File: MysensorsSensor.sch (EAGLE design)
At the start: 41 parts, among them IC1 TS5205, IC2 AT25DF512C-SSHN-B, IC3 ATSHA204A, Q1 FC-12M, U1 ATMEGA328P-AU

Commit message: 1. fix wrong boost converter footprint 2. connect led to A1 pin instead of A2 (which was used by the boost converter enable 3. change crystal footrint but not change the pcb
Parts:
- removed C11: 10u, rcl:C-EUC0603K
- removed Q1: FC-12M, crystal:FC-12M
- removed U$1: MCP1640, pulseoxparts:MCP1640
- added IC4: MCP1640CT-I/CHY, Microchip_By_element14_Batch_1:MCP1640CT-I/CHY
- added Q2: (no value), crystal:CRYSTALCTS406
- added R11: 1M, resistor:R-US_R0603
- C10, C4, C5, C6, C7: value (none) -> 100n
- C12: value (none) -> 10n
- C8, C9: value 10u -> 22p
- CR123A: value (none) -> BAT_PACKCR123A; device Battery:TAKACHI_BATT-CR123A -> batteries:BAT_PACKCR123A
- CR2032: value (none) -> 3V
- L1: value (none) -> 4.7u
- R1, R2, R3, R5, R7: value 100k -> 1M
- R10, R9: value 100k -> 10k
- R4: value 100k -> 620k
- R8: value 100k -> 1k
- renumbered LED1 to D1, P1 to X1, S1 to RST, S2 to BTN, SJ1 to J1, SJ2 to J2, SV4 to X2, U1 to IC5
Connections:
- net A1: now also R8.2
- net A2: now also IC4.EN, R11.1; no longer R8.2, U$1.EN
- net GND: now also IC4.GND, R11.2; no longer C11.2, U$1.GND
- net N$1: now also IC4.VFB; no longer U$1.VFB
- net N$2: now also Q2.1; no longer Q1.1
- net N$4: now also IC4.SW; no longer U$1.SW
- net N$6: now also Q2.2; no longer Q1.2
- net VBAT: now also IC4.VIN; no longer C11.1, U$1.VIN
- net VBOOST: now also IC4.VOUT; no longer U$1.VOUT
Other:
- moved on the sheet: C2, C3, CR123A, L1, R3, R4

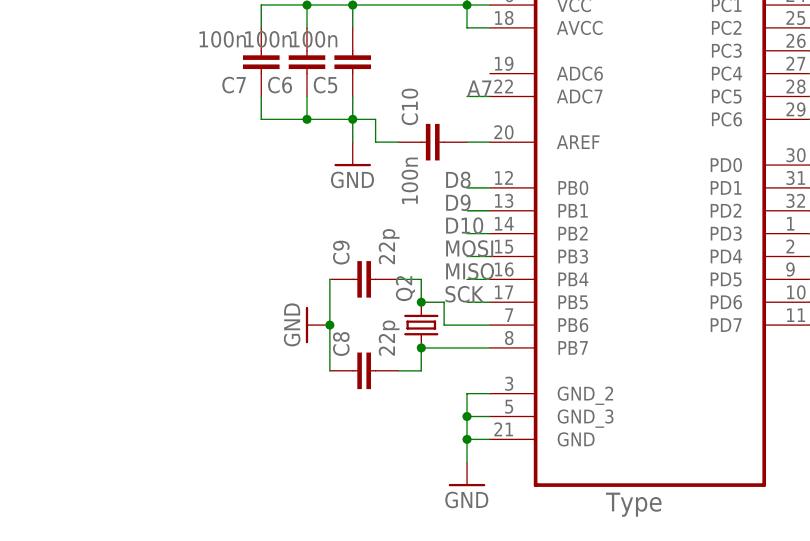
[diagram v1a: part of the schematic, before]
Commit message: 1. rearrange nfr24l01 connector and atmega328p chip
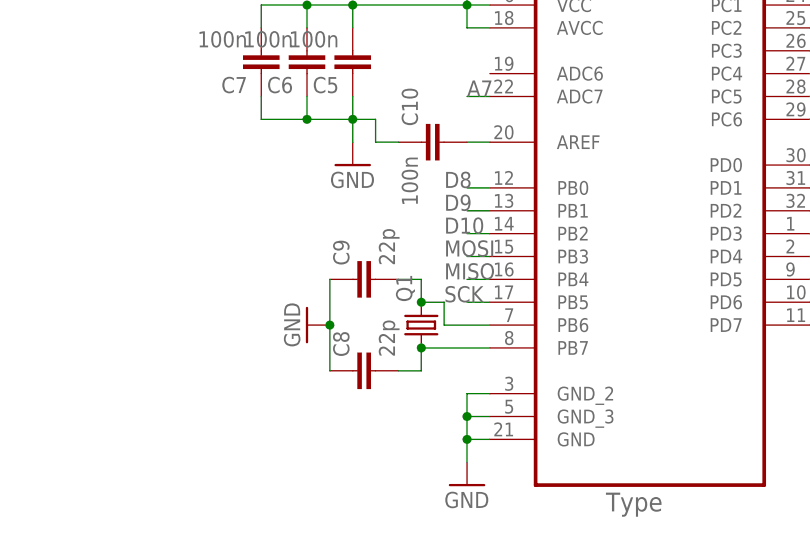
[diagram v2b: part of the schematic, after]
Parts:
- renumbered Q2 to Q1
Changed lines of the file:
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@@
 <part name="GND13" library="supply1" deviceset="GND" device=""/>
 <part name="IC4" library="Microchip_By_element14_Batch_1" deviceset="MCP1640CT-I/CHY" device=""/>
-<part name="Q2" library="crystal" deviceset="CRYSTAL" device="CTS406"/>
+<part name="Q1" library="crystal" deviceset="CRYSTAL" device="CTS406"/>
 </parts>
 <sheets>
@@
 <instance part="GND13" gate="1" x="-25.4" y="78.74"/>
 <instance part="IC4" gate="A" x="0" y="99.06"/>
-<instance part="Q2" gate="G$1" x="40.64" y="30.48" rot="R90"/>
+<instance part="Q1" gate="G$1" x="40.64" y="30.48" rot="R90"/>
 </instances>
 <busses>
@@
 <pinref part="C8" gate="G$1" pin="2"/>
 <wire x1="40.64" y1="25.4" x2="38.1" y2="25.4" width="0.1524" layer="91"/>
-<pinref part="Q2" gate="G$1" pin="1"/>
+<pinref part="Q1" gate="G$1" pin="1"/>
 <junction x="40.64" y="27.94"/>
 </segment>
@@
 <pinref part="C9" gate="G$1" pin="2"/>
 <wire x1="40.64" y1="35.56" x2="38.1" y2="35.56" width="0.1524" layer="91"/>
-<pinref part="Q2" gate="G$1" pin="2"/>
+<pinref part="Q1" gate="G$1" pin="2"/>
 <junction x="40.64" y="33.02"/>
 </segment>

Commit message: connect radio module irq with d2
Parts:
- IC1: value TS5205 -> APE8865Y5-30-HF-3
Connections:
- net D2: now also NRF24L01.IRQ
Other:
- moved on the sheet: C12, C13
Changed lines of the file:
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@@
 <part name="P+9" library="supply1" deviceset="VCC" device=""/>
 <part name="GND9" library="supply1" deviceset="GND" device=""/>
-<part name="IC1" library="v-reg" deviceset="TS5205" device=""/>
+<part name="IC1" library="v-reg" deviceset="TS5205" device="" value="APE8865Y5-30-HF-3"/>
 <part name="GND10" library="supply1" deviceset="GND" device=""/>
 <part name="C12" library="rcl" deviceset="C-EU" device="C0402" value="10n"/>
@@
 <instance part="IC1" gate="G$1" x="30.48" y="149.86"/>
 <instance part="GND10" gate="1" x="12.7" y="142.24"/>
-<instance part="C12" gate="G$1" x="43.18" y="142.24" rot="R180"/>
-<instance part="GND11" gate="1" x="43.18" y="137.16"/>
-<instance part="C13" gate="G$1" x="50.8" y="147.32"/>
+<instance part="C12" gate="G$1" x="53.34" y="142.24" rot="R180"/>
+<instance part="GND11" gate="1" x="53.34" y="137.16"/>
+<instance part="C13" gate="G$1" x="58.42" y="147.32"/>
 <instance part="P+2" gate="VCC" x="86.36" y="139.7"/>
 <instance part="C14" gate="G$1" x="12.7" y="152.4"/>
@@
 <pinref part="GND11" gate="1" pin="GND"/>
 <pinref part="C13" gate="G$1" pin="2"/>
-<wire x1="50.8" y1="142.24" x2="50.8" y2="139.7" width="0.1524" layer="91"/>
-<wire x1="50.8" y1="139.7" x2="43.18" y2="139.7" width="0.1524" layer="91"/>
-<junction x="43.18" y="139.7"/>
+<wire x1="58.42" y1="142.24" x2="58.42" y2="139.7" width="0.1524" layer="91"/>
+<wire x1="58.42" y1="139.7" x2="53.34" y2="139.7" width="0.1524" layer="91"/>
+<junction x="53.34" y="139.7"/>
 </segment>
 <segment>
@@
 <wire x1="129.54" y1="43.18" x2="129.54" y2="53.34" width="0.1524" layer="91"/>
 <label x="86.36" y="43.18" size="1.778" layer="95"/>
+<pinref part="NRF24L01" gate="G$1" pin="IRQ"/>
+<wire x1="165.1" y1="78.74" x2="139.7" y2="78.74" width="0.1524" layer="91"/>
+<wire x1="139.7" y1="78.74" x2="139.7" y2="43.18" width="0.1524" layer="91"/>
+<wire x1="139.7" y1="43.18" x2="129.54" y2="43.18" width="0.1524" layer="91"/>
+<junction x="129.54" y="43.18"/>
 </segment>
 </net>
@@
 <pinref part="IC1" gate="G$1" pin="CB"/>
 <pinref part="C12" gate="G$1" pin="2"/>
-<wire x1="40.64" y1="147.32" x2="43.18" y2="147.32" width="0.1524" layer="91"/>
+<wire x1="40.64" y1="147.32" x2="53.34" y2="147.32" width="0.1524" layer="91"/>
 </segment>
 </net>
@@
 <segment>
 <pinref part="IC1" gate="G$1" pin="VOUT"/>
-<label x="43.18" y="154.94" size="1.778" layer="95"/>
+<label x="58.42" y="154.94" size="1.778" layer="95"/>
 <pinref part="C13" gate="G$1" pin="1"/>
-<wire x1="40.64" y1="154.94" x2="50.8" y2="154.94" width="0.1524" layer="91"/>
-<wire x1="50.8" y1="154.94" x2="50.8" y2="149.86" width="0.1524" layer="91"/>
-</segment>
-<segment>
+<wire x1="40.64" y1="154.94" x2="58.42" y2="154.94" width="0.1524" layer="91"/>
+<wire x1="58.42" y1="154.94" x2="58.42" y2="149.86" width="0.1524" layer="91"/>
+</segment>
+<segment>

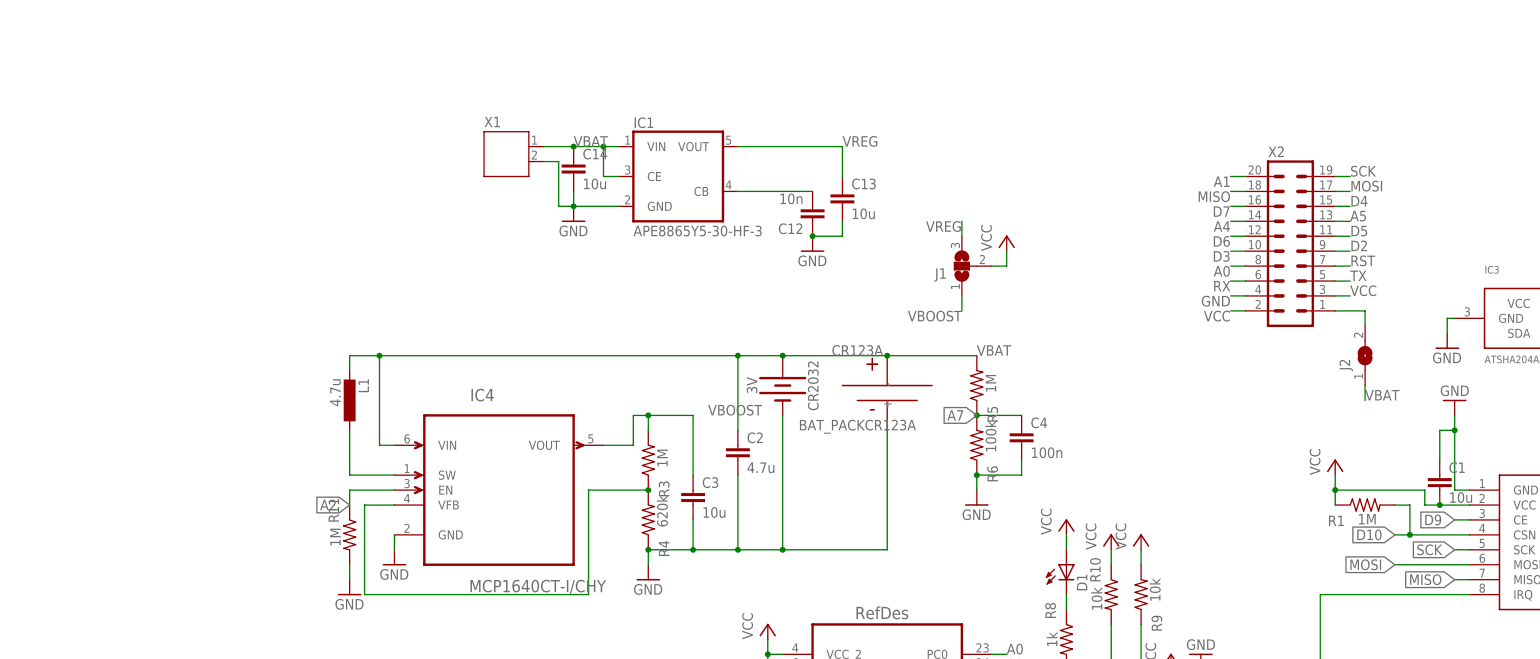
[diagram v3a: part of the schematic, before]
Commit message: use p-mosfet for reverse polarity
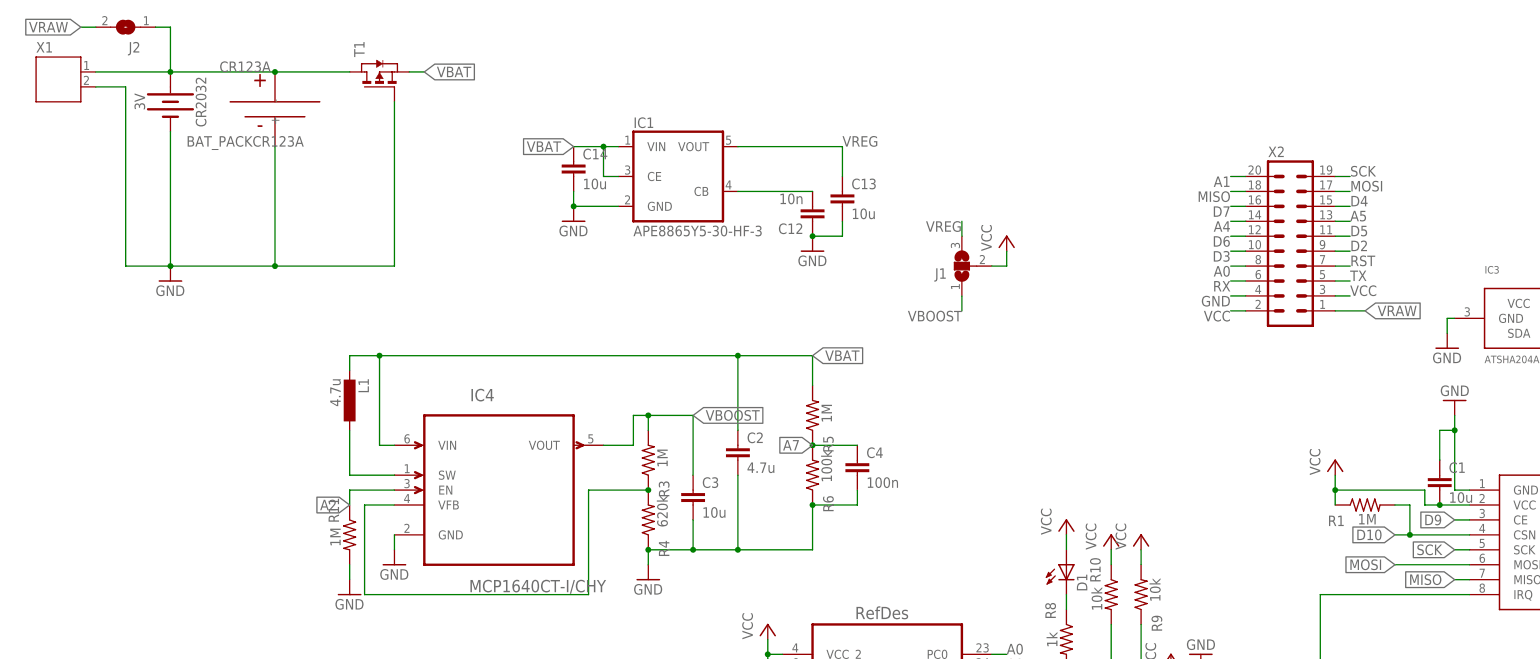
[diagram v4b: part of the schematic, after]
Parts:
- added T1: (no value), zetex:PMOSSOT23
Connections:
- net N$5 renamed VRAW
- new net N$7: CR123A.+, CR2032.+, J2.1, T1.D, X1.1
- net GND: now also T1.G
- net VBAT: now also T1.S; no longer CR123A.+, CR2032.+, J2.1, X1.1
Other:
- moved on the sheet: C4, CR123A, CR2032, J2, R5, R6, X1

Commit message: add RFM69
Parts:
- removed T1: (no value), zetex:PMOSSOT23
- added ANT: WIREPAD2,15/1,0, wirepad:WIREPAD2,15/1,0
- added Q2: FA-128, crystal:FA-128
- added RFM69W: RFM69HW, hoperf:RFM69HW
- C8, C9: device SparkFun-Passives:CAP0603-CAP -> SparkFun-Passives:CAP0402-CAP
- CR2032: value 3V -> (none); device SparkFun-Batteries:BATTERY-20MM_PTH -> Wurth_Elektronik_Electromechanic_Assembly_Spacer_rev15d:WA-BCPH_SMT_79527141
- Q1: device crystal:CRYSTALCTS406 -> zetex:PMOSSOT23
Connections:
- new net N$5: ANT.P, RFM69W.ANT
- net D10: now also RFM69W.NSS
- net D2: now also RFM69W.DIO0
- net GND: now also CR2032.NEG, Q1.G, Q2.2, Q2.4, RFM69W.GNDA, RFM69W.GNDB; no longer CR2032.-, T1.G
- net MISO: now also RFM69W.MISO
- net MOSI: now also RFM69W.MOSI
- net N$2: now also Q2.3; no longer Q1.1
- net N$6: now also Q2.1; no longer Q1.2
- net N$7: now also CR2032.POS, Q1.D; no longer CR2032.+, T1.D
- net SCK: now also RFM69W.SCK
- net VBAT: now also Q1.S; no longer T1.S
- net VCC: now also RFM69W.VCC
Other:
- moved on the sheet: C8, C9

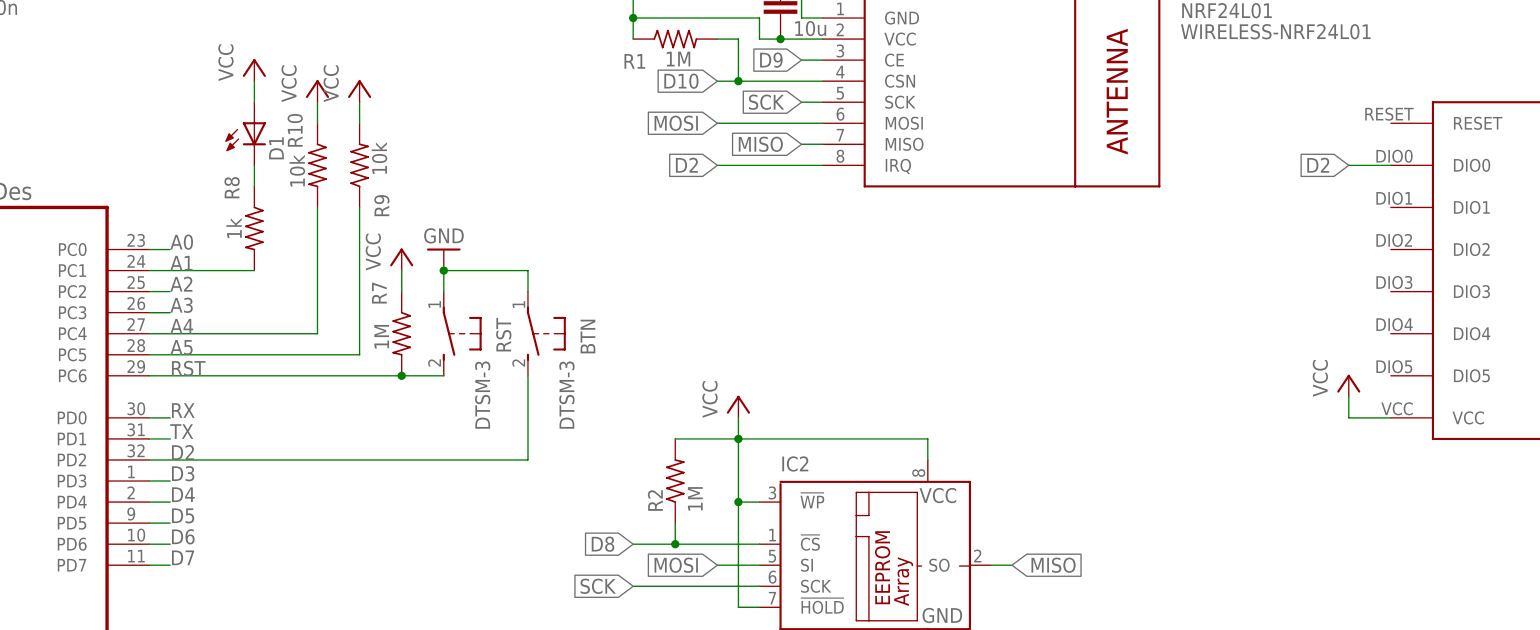
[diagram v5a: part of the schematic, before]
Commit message: add 0Ohm resistor for radio module interrupt + connect button to D3
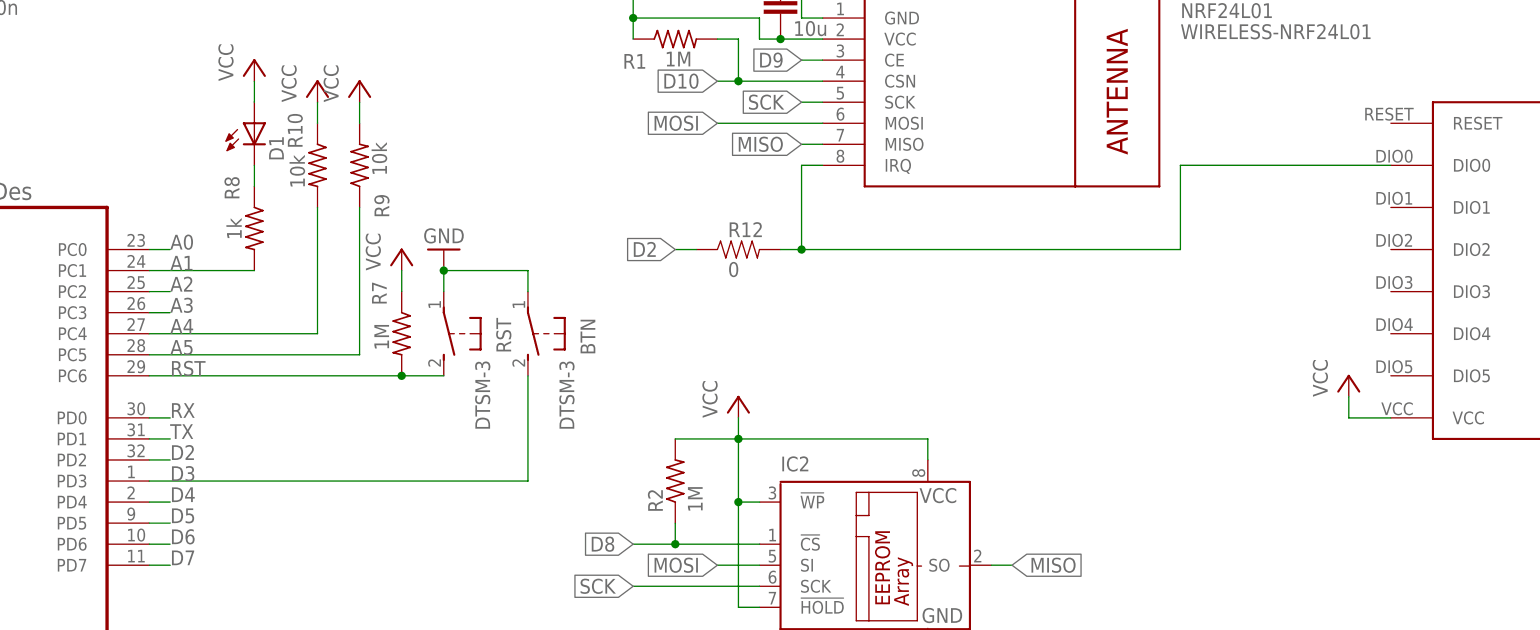
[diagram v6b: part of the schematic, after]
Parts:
- added R12: 0, SparkFun-Passives:RESISTOR0603-RES
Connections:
- new net N$9: NRF24L01.IRQ, R12.2, RFM69W.DIO0
- net D2: now also R12.1; no longer BTN.2, NRF24L01.IRQ, RFM69W.DIO0
- net D3: now also BTN.2
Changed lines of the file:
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@@
 <part name="CR2032" library="Wurth_Elektronik_Electromechanic_Assembly_Spacer_rev15d" deviceset="WA-BCPH" device="_SMT_79527141"/>
 <part name="Q2" library="crystal" deviceset="FA-" device="128"/>
+<part name="R12" library="SparkFun-Passives" deviceset="RESISTOR" device="0603-RES" value="0"/>
 </parts>
 <sheets>
@@
 <instance part="CR2032" gate="G$1" x="-55.88" y="152.4" rot="R270"/>
 <instance part="Q2" gate="G$1" x="38.1" y="30.48" rot="R270"/>
+<instance part="R12" gate="G$1" x="154.94" y="68.58" smashed="yes">
+<attribute name="NAME" x="153.67" y="70.0786" size="1.778" layer="95"/>
+<attribute name="VALUE" x="153.67" y="65.278" size="1.778" layer="96"/>
+</instance>
 </instances>
 <busses>
@@
 <segment>
 <pinref part="IC5" gate="A" pin="PD2"/>
-<pinref part="BTN" gate="G$1" pin="2"/>
-<wire x1="83.82" y1="43.18" x2="129.54" y2="43.18" width="0.1524" layer="91"/>
-<wire x1="129.54" y1="43.18" x2="129.54" y2="53.34" width="0.1524" layer="91"/>
+<wire x1="83.82" y1="43.18" x2="86.36" y2="43.18" width="0.1524" layer="91"/>
 <label x="86.36" y="43.18" size="1.778" layer="95"/>
 </segment>
 <segment>
-<pinref part="RFM69W" gate="A" pin="DIO0"/>
-<wire x1="233.68" y1="78.74" x2="228.6" y2="78.74" width="0.1524" layer="91"/>
-<label x="228.6" y="78.74" size="1.778" layer="95" rot="R180" xref="yes"/>
-</segment>
-<segment>
-<pinref part="NRF24L01" gate="G$1" pin="IRQ"/>
-<wire x1="165.1" y1="78.74" x2="152.4" y2="78.74" width="0.1524" layer="91"/>
-<label x="152.4" y="78.74" size="1.778" layer="95" rot="R180" xref="yes"/>
+<pinref part="R12" gate="G$1" pin="1"/>
+<wire x1="149.86" y1="68.58" x2="147.32" y2="68.58" width="0.1524" layer="91"/>
+<label x="147.32" y="68.58" size="1.778" layer="95" rot="R180" xref="yes"/>
 </segment>
 </net>
@@
 <segment>
 <pinref part="IC5" gate="A" pin="PD3"/>
-<wire x1="83.82" y1="40.64" x2="86.36" y2="40.64" width="0.1524" layer="91"/>
 <label x="86.36" y="40.64" size="1.778" layer="95"/>
+<pinref part="BTN" gate="G$1" pin="2"/>
+<wire x1="83.82" y1="40.64" x2="129.54" y2="40.64" width="0.1524" layer="91"/>
+<wire x1="129.54" y1="40.64" x2="129.54" y2="53.34" width="0.1524" layer="91"/>
 </segment>
 </net>
@@
 </segment>
 </net>
+<net name="N$9" class="0">
+<segment>
+<pinref part="RFM69W" gate="A" pin="DIO0"/>
+<wire x1="233.68" y1="78.74" x2="208.28" y2="78.74" width="0.1524" layer="91"/>
+<wire x1="208.28" y1="78.74" x2="208.28" y2="68.58" width="0.1524" layer="91"/>
+<pinref part="R12" gate="G$1" pin="2"/>
+<wire x1="208.28" y1="68.58" x2="162.56" y2="68.58" width="0.1524" layer="91"/>
+<pinref part="NRF24L01" gate="G$1" pin="IRQ"/>
+<wire x1="162.56" y1="68.58" x2="160.02" y2="68.58" width="0.1524" layer="91"/>
+<wire x1="165.1" y1="78.74" x2="162.56" y2="78.74" width="0.1524" layer="91"/>
+<wire x1="162.56" y1="78.74" x2="162.56" y2="68.58" width="0.1524" layer="91"/>
+<junction x="162.56" y="68.58"/>
+</segment>
+</net>
